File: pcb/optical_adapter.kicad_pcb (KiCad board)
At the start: 4 copper layers, 50 x 20 mm, 26 parts, among them J1 Conn_01x06_Pin, Q1 BC847, Q2 BC847, Q3 BC857, Q5 IRLML2060, U1 LM1117MP-3.3

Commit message: Fix #1
Increase the value of the power LED resistor since the LED was to
bright.
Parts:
- removed REF**: OSHW-Logo_5.7x6mm_Copper, Symbol:OSHW-Logo_5.7x6mm_Copper
- R9: value 5.6 -> 10

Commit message: Fix #5
Change D1 to Q4(phototransistor)
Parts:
- removed D1: D_Photo, footprints:kingbright_heli_r
- added Q4: Q_Photo_NPN, footprints:kingbright_heli_r, F.Cu at (127.5, 97.2)

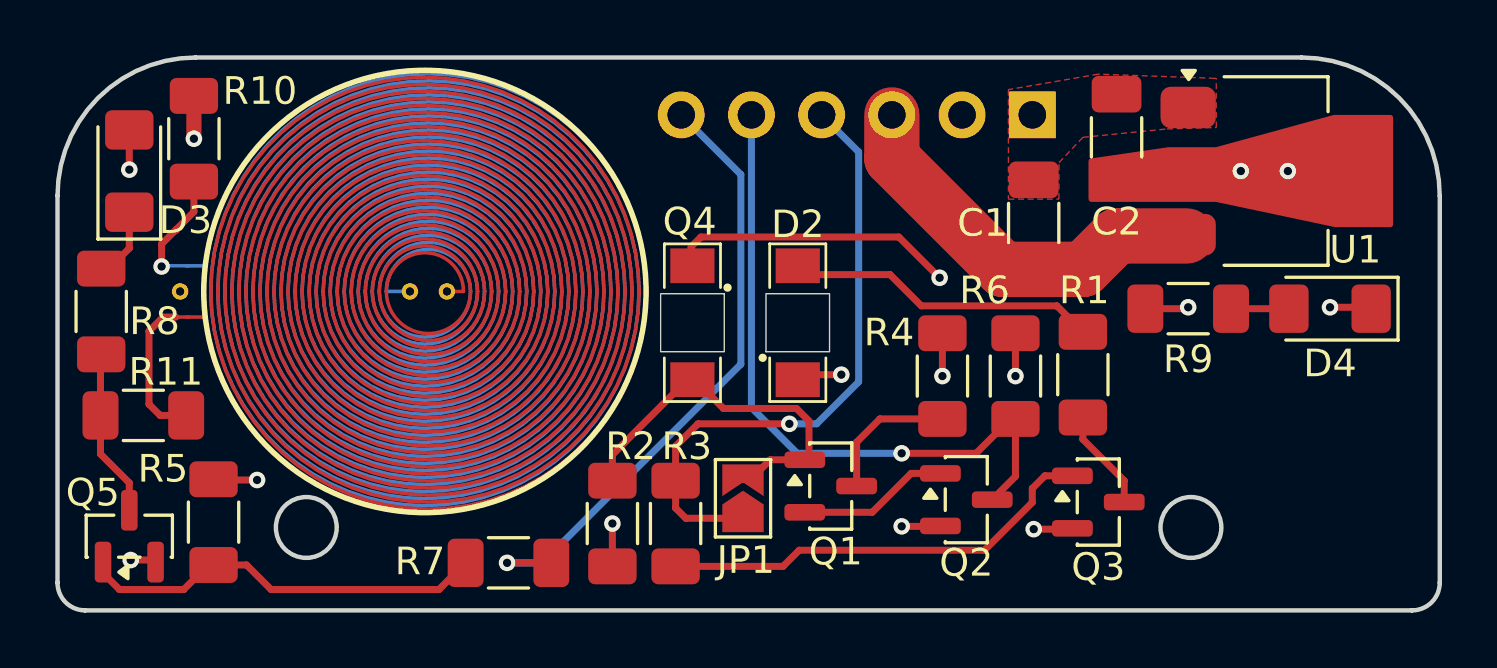
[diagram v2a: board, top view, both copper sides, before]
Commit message: Redesign RX circuit
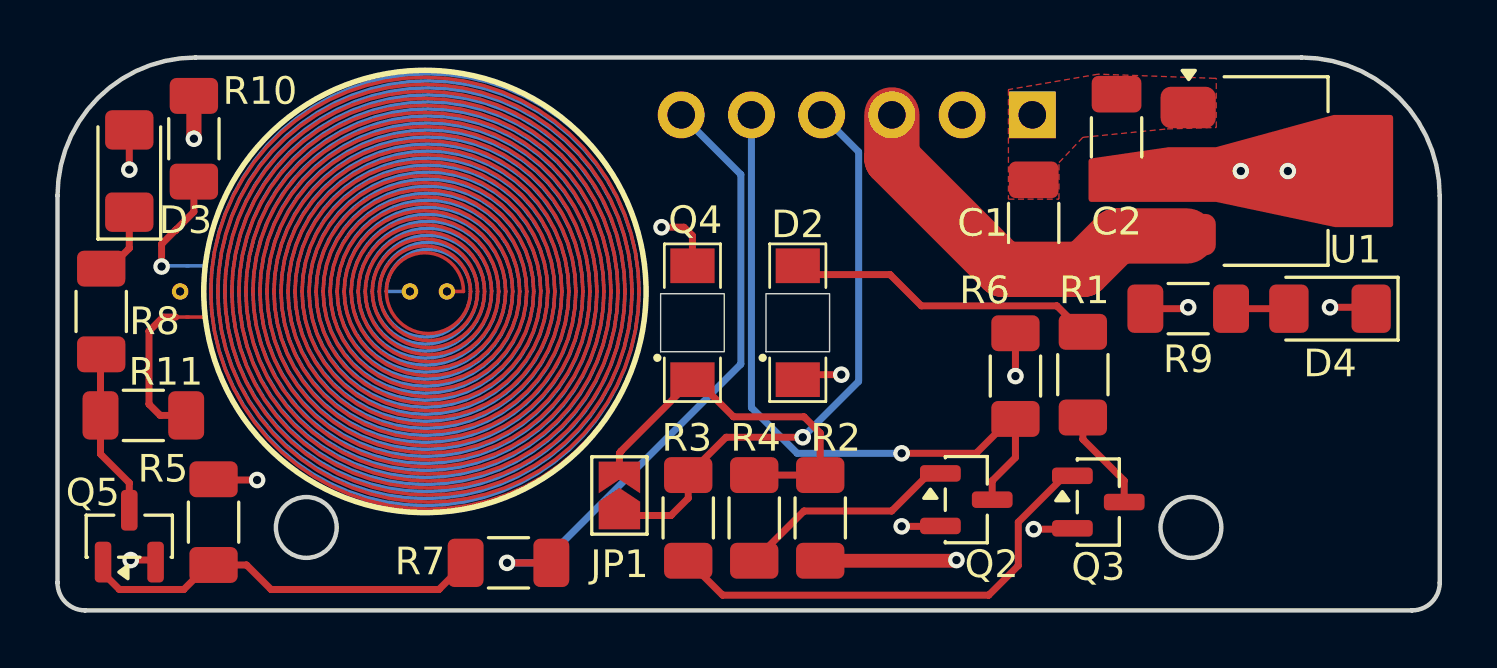
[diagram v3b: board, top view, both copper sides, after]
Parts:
- removed Q1: BC847, Package_TO_SOT_SMD:SOT-23
- R4: value 10k -> 1k
- moved R4 8.52 mm to (129.7, 104.2)
- moved R2 7.52 mm to (132.1, 104.2), turned to 90 degrees
- moved JP1 4.47 mm to (124.9, 103.4)
- moved R3 0.50 mm to (127.4, 104.2)
- turned Q4 to 90 degrees
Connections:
- Q2 pad 1: Net-(Q1-E) -> Net-(Q2-B)
- Q4 pad 1: +3V3 -> Net-(JP1-B)
- Q4 pad 2: Net-(JP1-B) -> GND
- R2 pad 1: Net-(JP1-B) -> +3V3
- R2 pad 2: GND -> Net-(JP1-B)
- R4 pad 1: +3V3 -> Net-(JP1-B)
- R4 pad 2: Net-(Q1-C) -> Net-(Q2-B)
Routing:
- net Net-(Q2-B): track 0.00 -> 8.04 mm
- net +3V3: track 16.8 -> 9.41 mm, vias 7 -> 6
- net Net-(Q1-E): track 5.49 -> 0.00 mm
- net Net-(Q1-C): track 5.04 -> 0.00 mm
- net /TX: track 22.6 -> 21.3 mm
- net Net-(Q3-B): track 16.0 -> 17.1 mm
- net GND: track 8.84 -> 9.63 mm
